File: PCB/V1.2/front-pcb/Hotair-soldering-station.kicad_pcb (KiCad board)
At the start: 2 copper layers, 99.4 x 61 mm, 24 parts, among them J1 Conn_01x03, J2 main-board-conn, J3 hot_on, SW1 HOTAIR_UP, SW2 HOTAIR_DOWN, SW3 SIRON_UP, SW4 SIRON_DOWN, SW5 FAN_UP, SW6 FAN_DOWN, SW7 MENU_UP, SW8 MENU_DOWN, SW9 MENU_OK

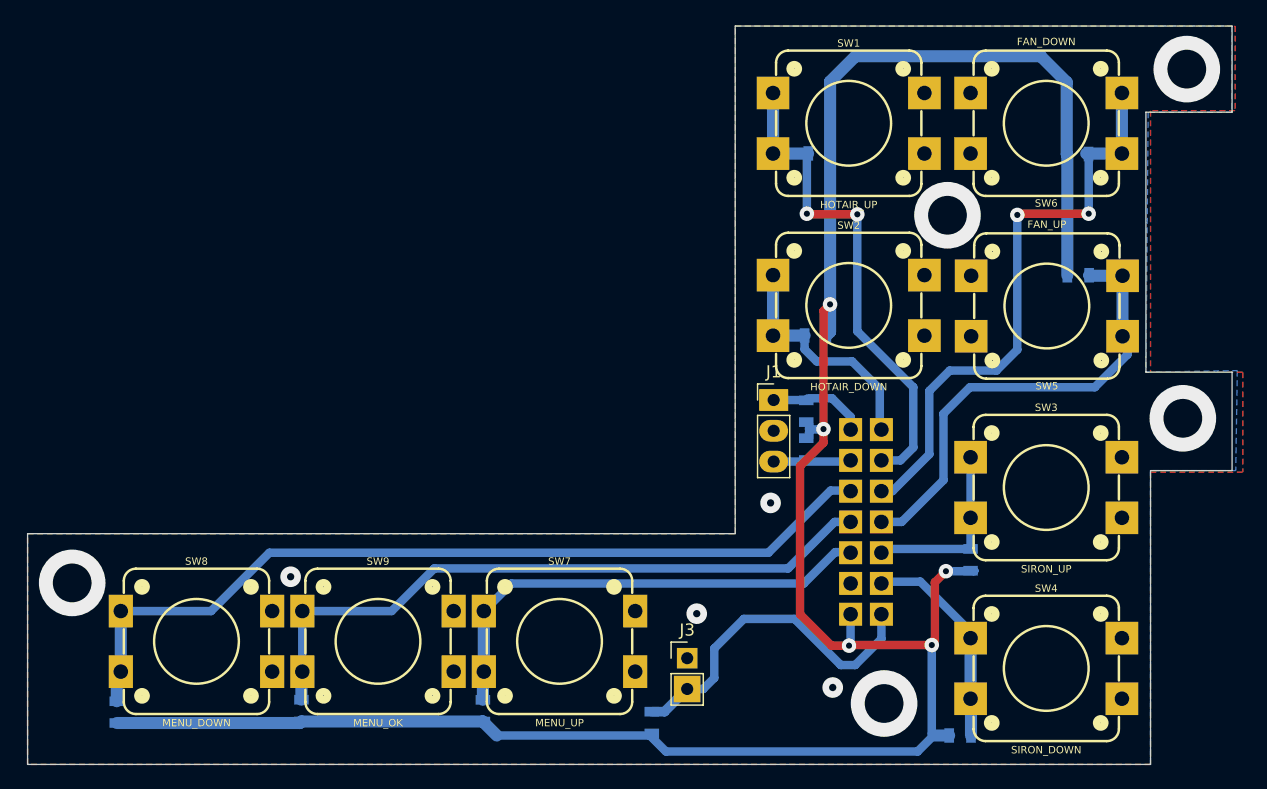
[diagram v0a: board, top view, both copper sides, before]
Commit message: T12 and WEP tests done
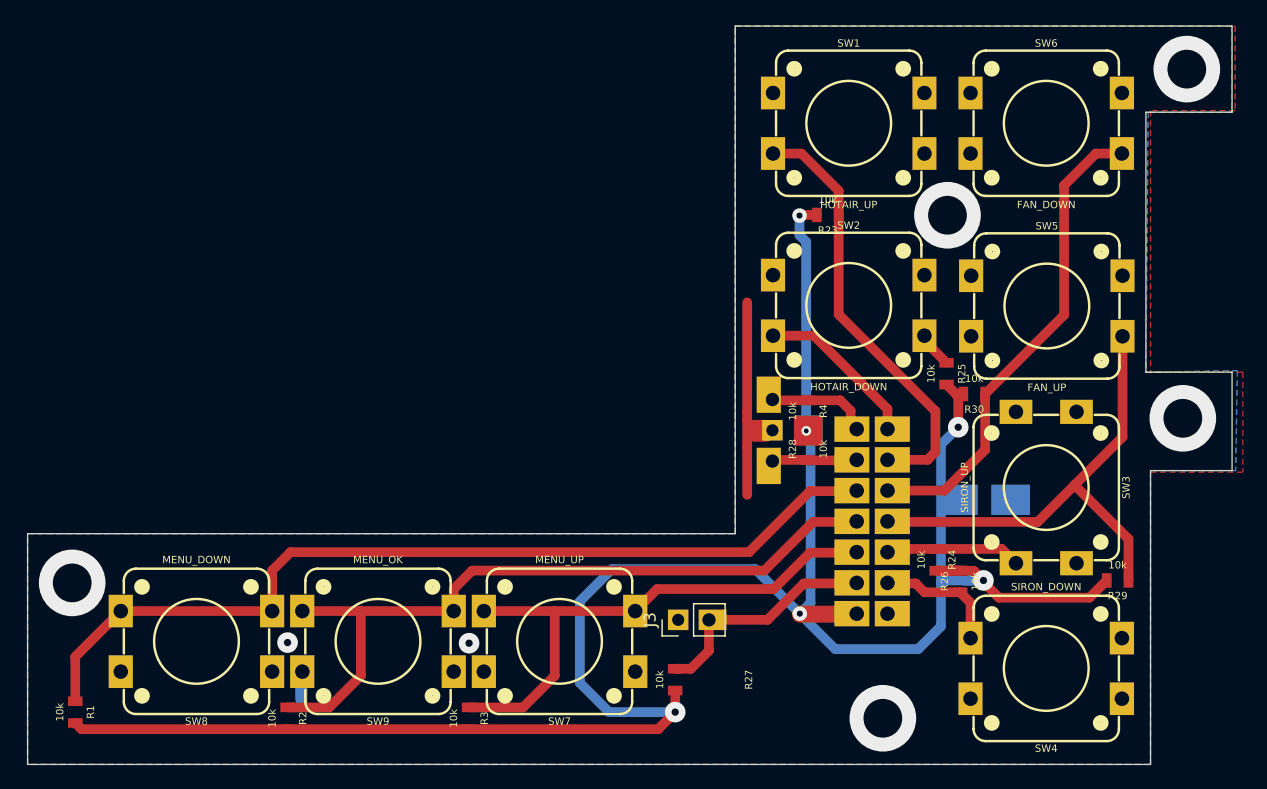
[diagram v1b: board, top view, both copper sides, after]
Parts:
- added C1: C_Polarized, Capacitors_Tantalum_SMD:CP_Tantalum_Case-B_EIA-3528-21_Hand, B.Cu at (153.3, 63.2)
- J1: moved to B.Cu
- J2: footprint My-Footprints:Con-01x14 -> My-Footprints:IDC-Header_2x07_P2.54mm_Vertical
- R1, R2, R23, R24, R25, R26, R27, R28, R29, R3, R30, R4: moved to F.Cu
- SW1, SW2, SW3, SW4, SW5, SW6: footprint Switches:TACTILE_SWITCH_PTH_12MM -> My-Footprints:TACTILE_SWITCH_PTH_12MM
- moved R29 25.4 mm to (164.3, 69.9)
- moved R30 21.6 mm to (152.5, 54.5)
- moved R26 12.7 mm to (151.3, 70.0), turned to 90 degrees
- moved R25 11.3 mm to (150.2, 52.8), turned to -90 degrees
- moved R23 5.13 mm to (140.4, 39.7), turned to 180 degrees
- moved R27 4.03 mm to (127.8, 78.1)
- moved R1 3.43 mm to (78.2, 80.8)
- moved J3 3.26 mm to (128.0, 73.2), turned to 90 degrees
- moved J2 2.96 mm to (142.7, 72.6)
- moved R24 2.79 mm to (149.4, 68.2)
- moved R2 1.31 mm to (95.8, 81.3)
- moved R3 1.30 mm to (110.7, 81.3)
- moved R28 0.15 mm to (138.7, 59.1)
- moved R4 0.15 mm to (138.7, 55.9)
- moved J1 0.11 mm to (135.8, 55.0), turned to 180 degrees
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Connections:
- J2 pad 14: HOTAIR_ON_SW -> GND
- J2 pad 2: GND -> HOTAIR_ON_SW
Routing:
- net GND: track 0.00 -> 20.5 mm, vias 9 -> 7
- net HOTAIR_FAN_DOWN_SW: track 49.1 -> 39.9 mm, vias 2 -> 0
- net HOTAIR_ON_SW: track 28.1 -> 18.9 mm
- net SOLDER_DOWN_SW: track 17.4 -> 10.9 mm
- net MENU_UP_SW: track 39.5 -> 45.8 mm
- net MENU_OK_SW: track 55.7 -> 61.9 mm
- net HOTAIR_UP_SW: track 41.3 -> 35.8 mm, vias 2 -> 0
- net MENU_DOWN_SW: track 72.1 -> 75.3 mm
- net HOTAIR_DOWN_SW: track 19.9 -> 16.7 mm
- net SOLDER_UP_SW: track 15.0 -> 12.2 mm
- net HOTAIR_FAN_UP_SW: track 38.4 -> 40.8 mm
- net +3V3: track 189.0 -> 187.2 mm, vias 5 -> 6

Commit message: Main and front PCB schematic rearrangement.
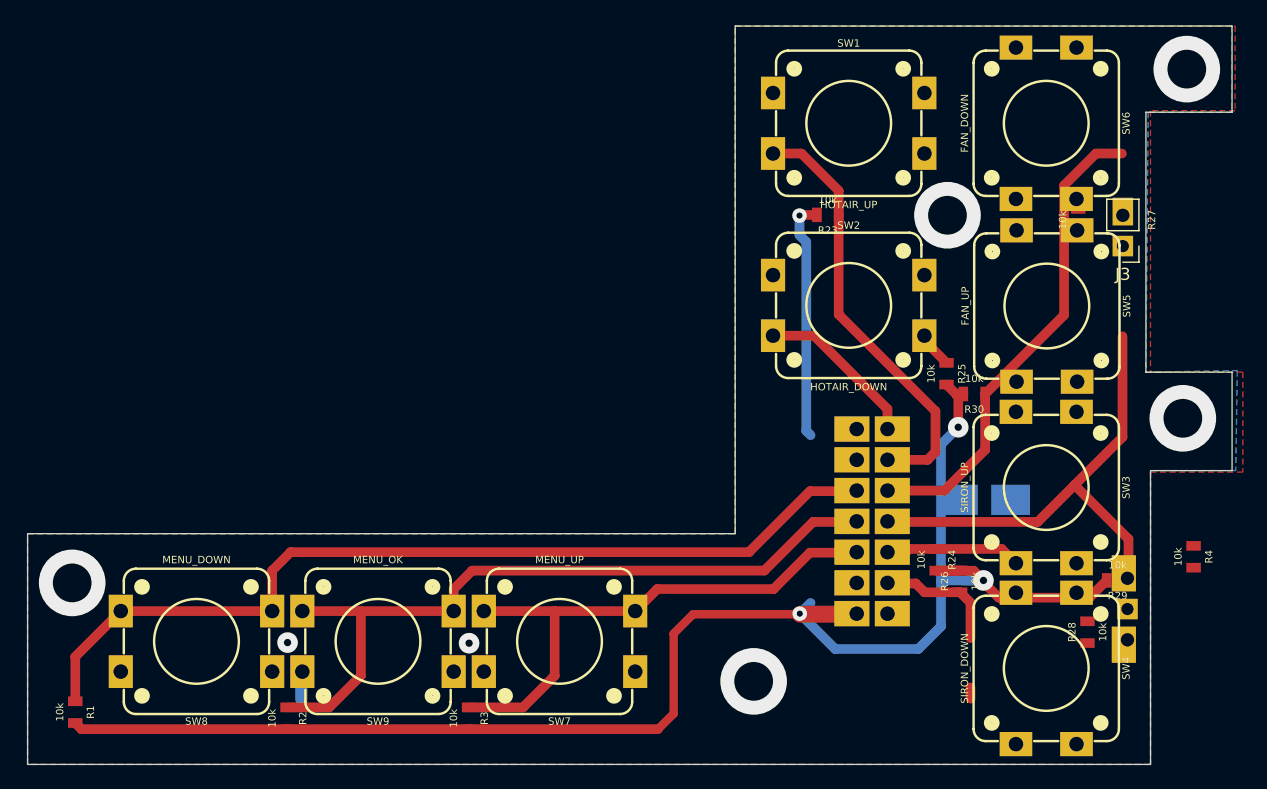
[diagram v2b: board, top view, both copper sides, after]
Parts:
- moved R27 50.5 mm to (161.0, 40.1)
- moved J3 48.0 mm to (164.7, 42.3), turned to 180 degrees
- moved R4 34.0 mm to (170.6, 67.9)
- moved J1 32.8 mm to (165.1, 69.7)
- moved R28 27.6 mm to (161.8, 74.2)
- turned SW4 to -90 degrees
- turned SW5 to -90 degrees
- turned SW6 to -90 degrees
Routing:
- net +3V3: track 187.2 -> 151.4 mm, vias 6 -> 4
- net HOTAIR_ON_SW: track 18.9 -> 0.00 mm
- net GND: track 20.5 -> 3.32 mm
- net WEP_ON_SW: track 8.28 -> 0.00 mm
- net T12_ON_SW: track 6.42 -> 0.00 mm

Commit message: Front panel rocker switch connector change, preparing pcb for production
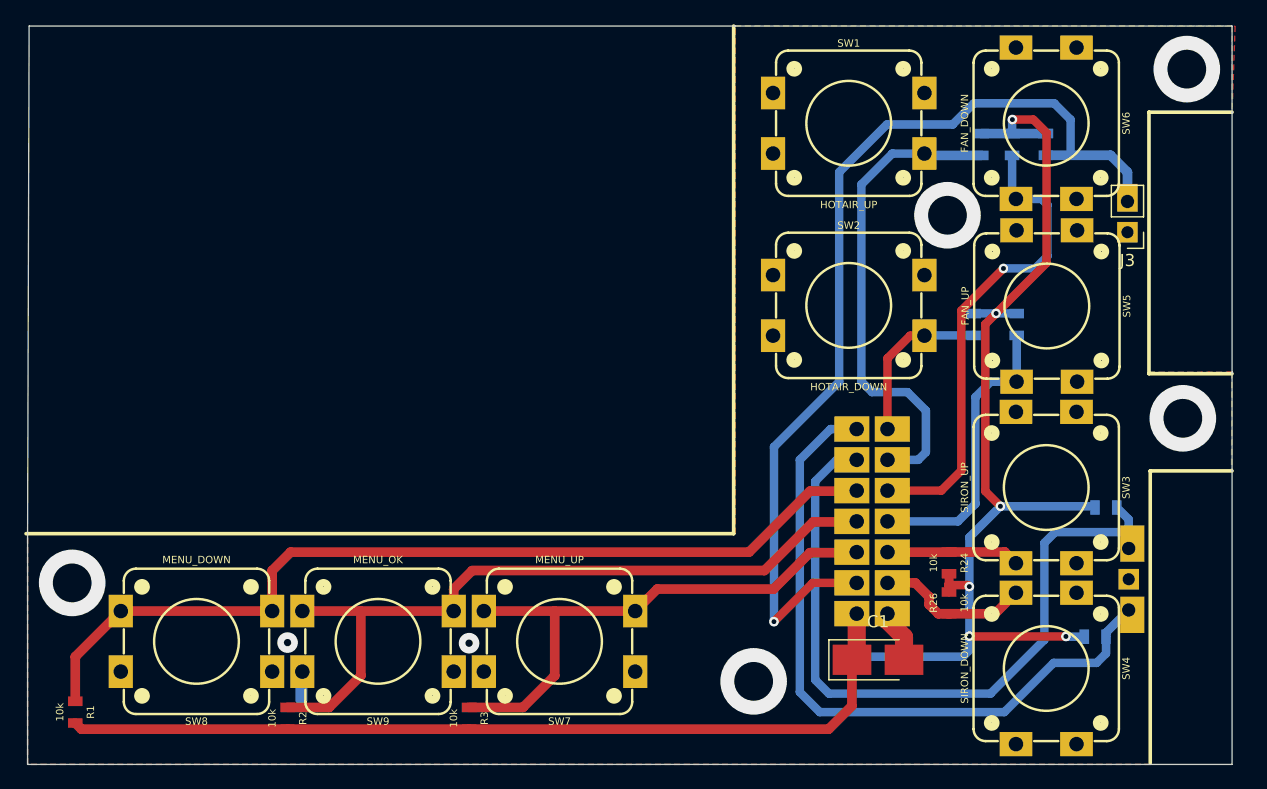
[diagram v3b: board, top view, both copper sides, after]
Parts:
- C1: moved to F.Cu
- R23, R25, R27, R28, R29, R30, R4: moved to B.Cu
- moved R29 22.7 mm to (156.0, 48.8), turned to 90 degrees
- moved R30 20.8 mm to (155.6, 33.9), turned to 90 degrees
- moved C1 15.9 mm to (144.5, 76.5)
- moved R23 13.9 mm to (153.0, 33.9), turned to 90 degrees
- moved R4 10.5 mm to (162.4, 74.5), turned to 180 degrees
- moved R28 10.4 mm to (163.3, 63.9), turned to 180 degrees
- moved R27 6.78 mm to (158.4, 33.9), turned to 90 degrees
- moved R25 4.64 mm to (152.4, 48.8), turned to 90 degrees
- moved J1 2.62 mm to (165.2, 72.3), turned to 0 degrees
- moved R26 2.00 mm to (150.4, 71.8)
- moved J3 1.20 mm to (165.1, 41.2)
- moved R24 1.05 mm to (150.4, 68.5)
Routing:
- net HOTAIR_ON_SW: track 0.00 -> 82.2 mm, vias 0 -> 1
- net T12_ON_SW: track 0.00 -> 61.1 mm
- net WEP_ON_SW: track 0.00 -> 57.3 mm
- net +3V3: track 151.4 -> 168.0 mm, vias 4 -> 6
- net HOTAIR_FAN_UP_SW: track 40.8 -> 24.4 mm
- net HOTAIR_UP_SW: track 35.8 -> 40.5 mm
- net GND: track 3.32 -> 7.28 mm
- net HOTAIR_DOWN_SW: track 16.7 -> 14.3 mm
- net SOLDER_DOWN_SW: track 10.9 -> 12.8 mm
- net SOLDER_UP_SW: track 12.2 -> 11.0 mm
- net HOTAIR_FAN_DOWN_SW: track 39.9 -> 39.7 mm, vias 0 -> 1
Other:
- outline, holes or cut-outs redrawn

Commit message: Front panel done
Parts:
- added G***: LOGO, graphic:open-source-HW-10x10, B.Cu at (142.0, 39.0)
- added G***: LOGO, graphic:honeybadger2, B.Cu at (88.3, 74.9)
- C1: value C_Polarized -> 10u
- J2: renamed from J1; value Conn_01x03 -> SOLDER_ON_SW
- J3: value hot_on -> HOTAIR_ON_SW; moved to B.Cu
- SW1: renamed from SW7; value MENU_UP -> MENU_RIGHT
- SW2: renamed from SW8; value MENU_DOWN -> MENU_LEFT
- SW4: renamed from SW3; value SIRON_UP -> SOLDER_UP_TEMP
- SW5: renamed from SW4; value SIRON_DOWN -> SOLDER_DOWN_TEMP
- SW8: renamed from SW1; value HOTAIR_UP -> HOTAIR_UP_TEMP
- SW9: renamed from SW2; value HOTAIR_DOWN -> HOTAIR_DOWN_TEMP
- turned J3 to 0 degrees
- renumbered J2 to J1, R30 to R10, R25 to R11, R27 to R12, R24 to R4, R28 to R5, R26 to R6, R4 to R7, R29 to R8, R23 to R9, SW9 to SW3, SW5 to SW6, SW6 to SW7
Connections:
- net MENU_DOWN_SW renamed MENU_LEFT_SW
- net MENU_UP_SW renamed MENU_RIGHT_SW
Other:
- board text added: "FRONT PANEL CONNECTOR"
- board text added: "FRONT PCB V1.2 05.2022"
- board text added: "SHW-01 HOTAIR/SOLDERING STATION"
